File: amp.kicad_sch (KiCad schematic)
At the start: 0 parts

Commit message: amp and sd sheets revision 1
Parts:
- added C5: 10u, symbol Device:C
- added C6: 0.1u, symbol Device:C
- added C7, C8: 220p, symbol Device:C
- added LS1: 8Ω, symbol Device:Speaker
- added U2: MAX98357A, Package_DFN_QFN:TQFN-16-1EP_3x3mm_P0.5mm_EP1.23x1.23mm, symbol Audio:MAX98357A
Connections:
- new net: C7.1, LS1.2, U2.10 (OUTN)
- new net: C8.1, LS1.1, U2.9 (OUTP)
- new net: C5.2, C6.2, U2.7 (VDD), U2.8 (VDD)
- new net BCLK: U2.16 (BCLK)
- new net DIN: U2.1 (DIN)
- new net GND: C7.2, C8.2, U2.11 (GND), U2.15 (GND), U2.2 (GAIN_SLOT), U2.3 (GND)
- new net LRCLK: U2.14 (LRCLK)
- new net VDD33: C5.1, C6.1
- no-connect marks 0 -> 2

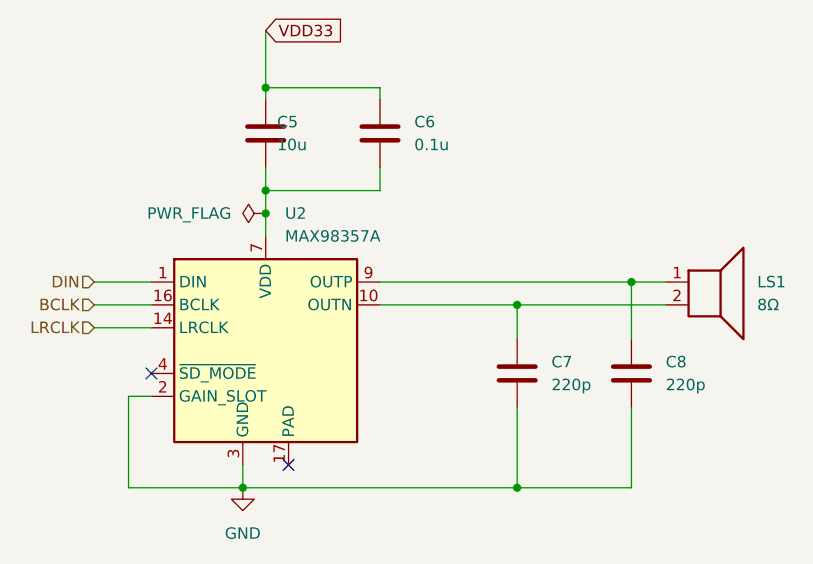
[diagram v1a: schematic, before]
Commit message: rfid revision 1 sch
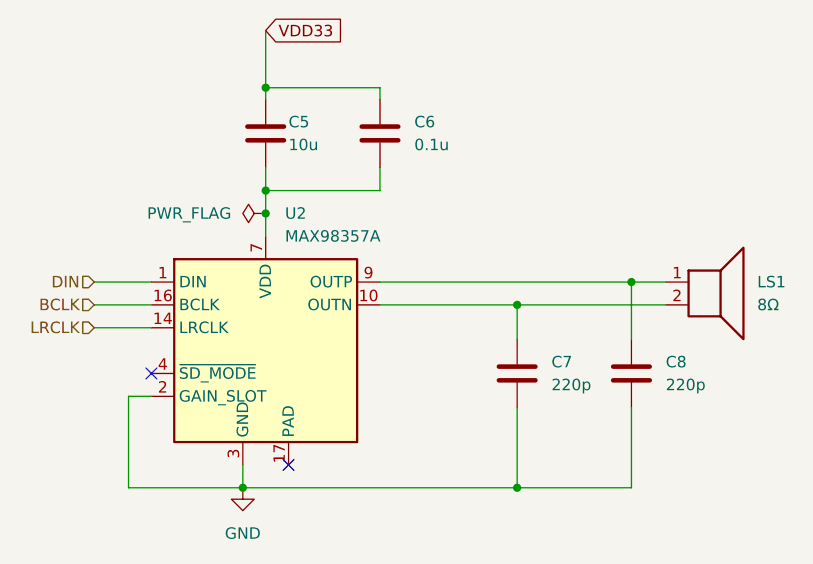
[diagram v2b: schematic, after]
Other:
- company: (none) -> C.Boerner
- title: (none) -> Amplifier Module
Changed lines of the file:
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@@
 	(generator_version "9.0")
 	(paper "A4")
+	(title_block
+		(title "Amplifier Module")
+		(date "2025-07-22")
+		(rev "1.0")
+		(company "C.Boerner")
+	)
 	(junction
 		(at 165.1 81.28)
@@
 		(pin "1"
 		)
-		(instances
-			(project ""
-				(path "/d400bd10-35e9-4717-b347-ccb991be6072/58aa8eb1-6419-4649-9641-e1795f62a7f1"
-					(reference "LS1")
-					(unit 1)
-				)
-			)
-		)
 	)
 	(symbol
@@
 		(dnp no)
 		(property "Reference" "C5"
-			(at 138.43 60.9599 0)
+			(at 139.7 60.96 0)
 			(effects
 				(font
@@
 		)
 		(property "Value" "10u"
-			(at 138.43 63.4999 0)
+			(at 139.7 63.5 0)
 			(effects
 				(font
@@
 		)
 		(pin "1"
-		)
-		(instances
-			(project ""
-				(path "/d400bd10-35e9-4717-b347-ccb991be6072/58aa8eb1-6419-4649-9641-e1795f62a7f1"
-					(reference "C5")
-					(unit 1)
-				)
-			)
 		)
 	)
@@
 		(pin "13"
 		)
-		(instances
-			(project ""
-				(path "/d400bd10-35e9-4717-b347-ccb991be6072/58aa8eb1-6419-4649-9641-e1795f62a7f1"
-					(reference "U2")
-					(unit 1)
-				)
-			)
-		)
-	)
+	)
